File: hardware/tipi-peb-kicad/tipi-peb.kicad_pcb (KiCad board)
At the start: 2 copper layers, 237.7 x 117.3 mm, 43 parts, among them Q1 Q_NPN_BCE, U1 74HCT138, U2 27C256, U3 74HCT244, U4 74HCT244, U5 74HCT244, U6 XC95144XL-TQ100, U7 74HCT245, U8 LM1117-3.3, U9 LM7805_TO220

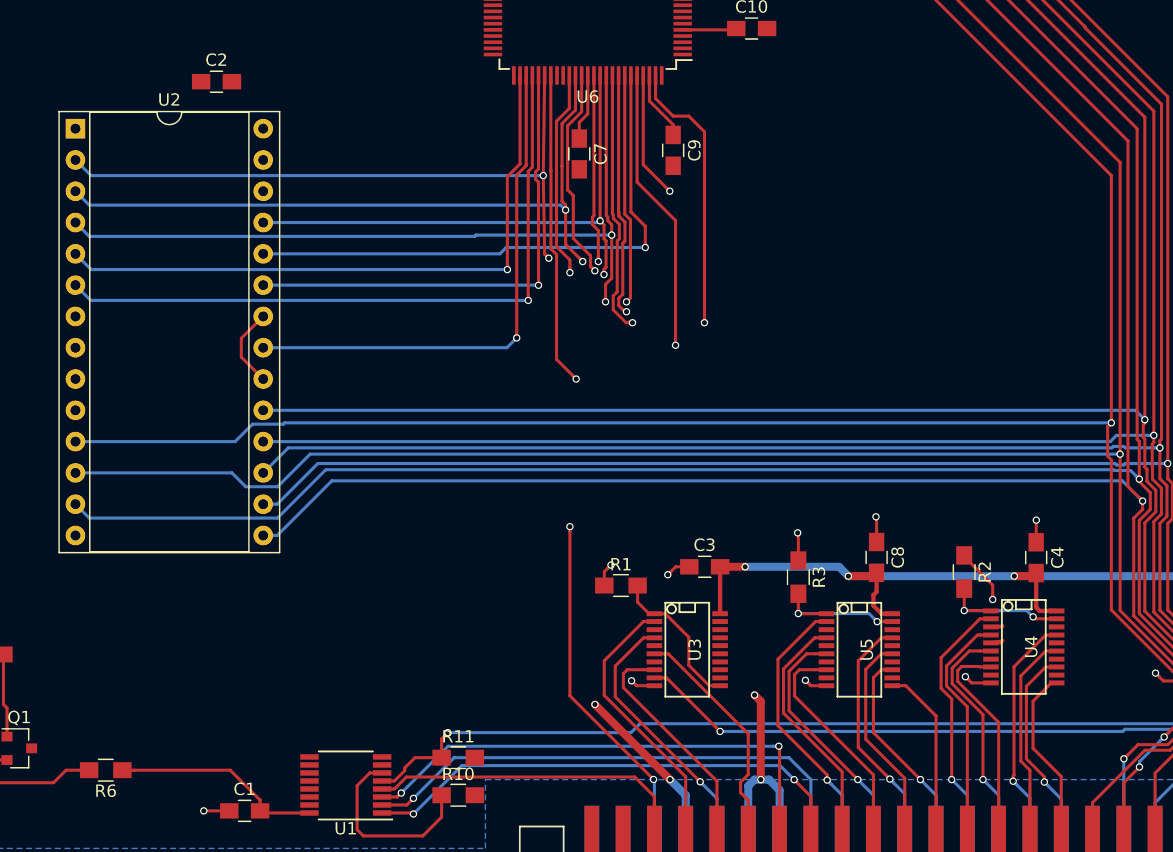
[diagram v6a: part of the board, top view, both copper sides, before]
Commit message: finish an address buffer
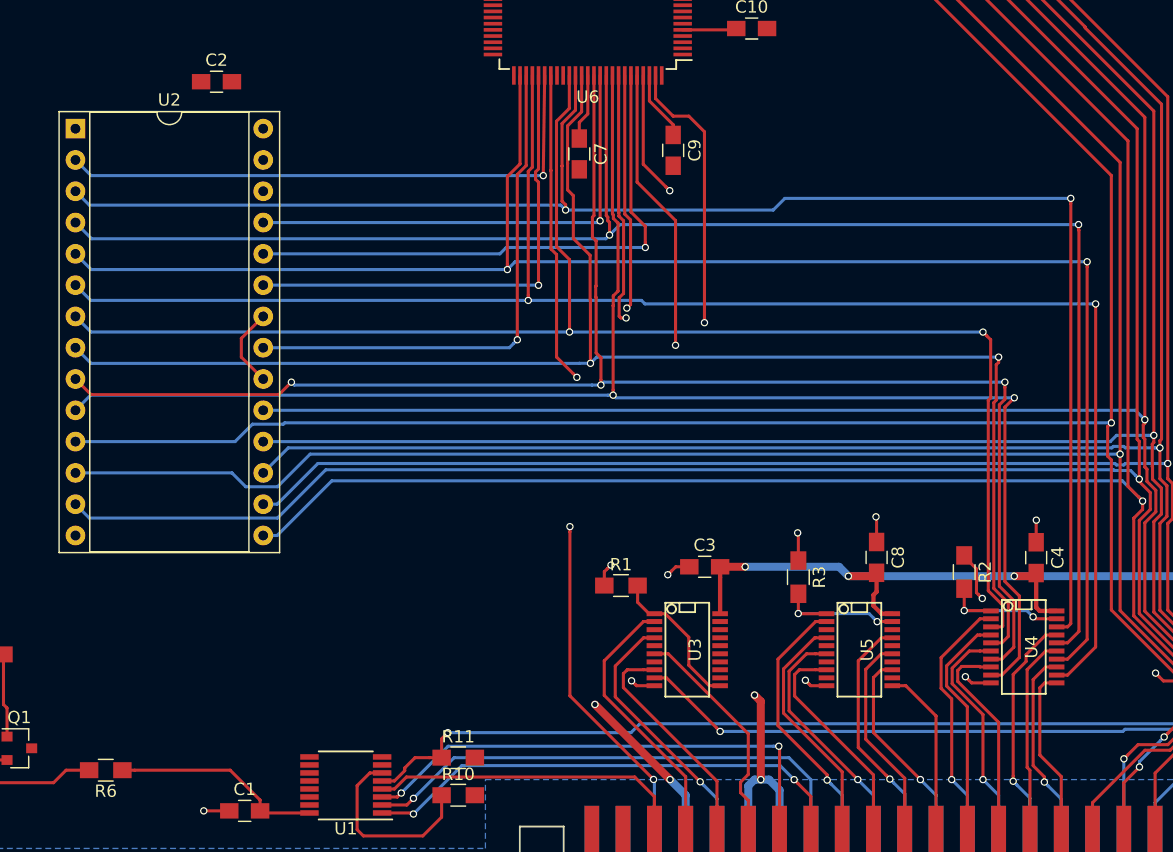
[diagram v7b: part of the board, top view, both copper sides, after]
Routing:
- net B_A14: track 15.4 -> 126.5 mm, vias 1 -> 3
- net B_A15: track 21.5 -> 127.9 mm, vias 1 -> 2
- net B_A13: track 19.2 -> 125.2 mm, vias 1 -> 2
- net B_A12: track 18.8 -> 121.6 mm, vias 1 -> 2
- net B_A10: track 51.8 -> 132.9 mm, vias 1 -> 2
- net B_A11: track 55.7 -> 133.8 mm, vias 1 -> 2
- net B_A8: track 56.7 -> 129.1 mm
- net B_A9: track 62.8 -> 130.7 mm
- net B_A3: track 53.5 -> 46.6 mm, vias 2 -> 1
- net B_A7: track 43.8 -> 39.2 mm, vias 2 -> 1
- net B_A2: track 19.9 -> 20.5 mm

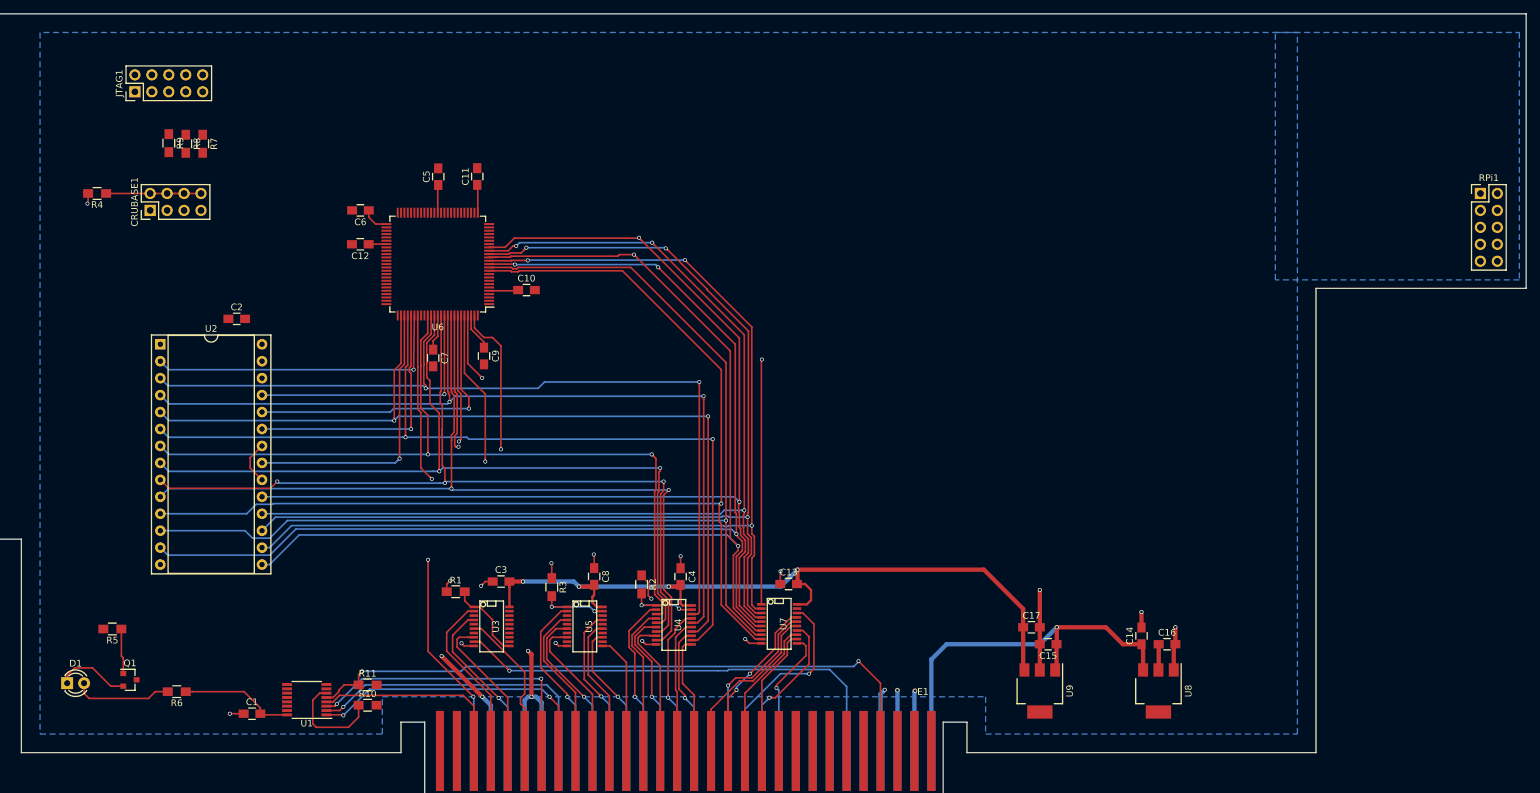
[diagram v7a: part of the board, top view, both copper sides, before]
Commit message: just power lines left
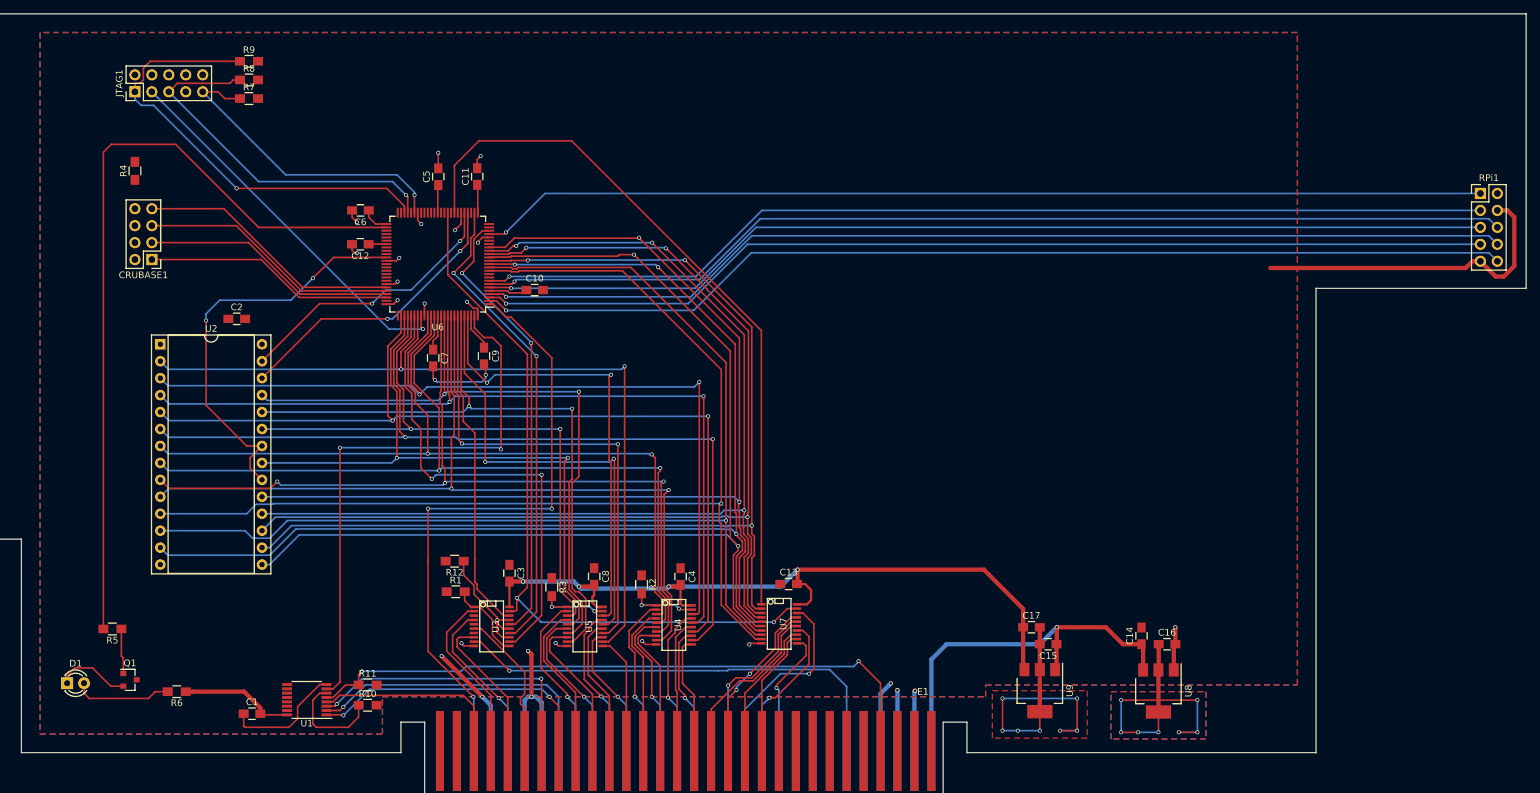
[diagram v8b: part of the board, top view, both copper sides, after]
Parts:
- added R12: 1k, Resistors_SMD:R_0805_HandSoldering, F.Cu at (168.6, 148.1)
- U8, U9: footprint TO_SOT_Packages_SMD:SOT-223 -> TO_SOT_Packages_SMD:SOT-223-3_TabPin2
- moved R9 17.2 mm to (137.7, 73.2), turned to 0 degrees
- moved R8 13.5 mm to (137.7, 75.9), turned to 0 degrees
- moved R7 9.70 mm to (137.7, 78.7), turned to 0 degrees
- moved CRUBASE1 7.37 mm to (123.2, 102.9), turned to 180 degrees
- moved R4 6.60 mm to (120.7, 89.6), turned to 90 degrees
- moved C3 1.77 mm to (176.8, 149.9), turned to 270 degrees
- moved C10 1.23 mm to (180.6, 107.4)
- moved U9 0.05 mm to (256.3, 167.5)
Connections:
- U3 pad 13: Net-(U3-Pad13) -> Net-(R12-Pad1)
- U3 pad 15: Net-(U3-Pad15) -> Net-(R12-Pad1)
- U3 pad 17: Net-(U3-Pad17) -> Net-(R12-Pad1)
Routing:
- net R_DC: track 0.00 -> 155.8 mm, vias 0 -> 1
- net R_DOUT: track 0.00 -> 155.7 mm, vias 0 -> 1
- net R_DIN: track 0.00 -> 155.6 mm, vias 0 -> 1
- net R_RT: track 0.00 -> 153.0 mm, vias 0 -> 1
- net R_RESET: track 0.00 -> 152.6 mm, vias 0 -> 1
- net R_LE: track 0.00 -> 152.4 mm, vias 0 -> 1
- net R_CLK: track 0.00 -> 151.1 mm, vias 0 -> 1
- net LED0: track 0.00 -> 119.5 mm
- net GND: track 124.7 -> 243.4 mm, vias 23 -> 33
- net DB_EN: track 0.00 -> 110.6 mm, vias 0 -> 2
- net B_A3: track 46.6 -> 122.3 mm, vias 1 -> 2
- net B_PH3: track 0.00 -> 71.7 mm, vias 0 -> 2
- net DB_DIR: track 36.7 -> 107.4 mm, vias 1 -> 0
- net JTAG_TCK: track 0.00 -> 68.5 mm, vias 0 -> 1
- net B_CRUCLK: track 0.00 -> 67.5 mm, vias 0 -> 2
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- added copper zone on B.Cu, net +3V3
- added copper zone on F.Cu, net +3V3
- added copper zone on F.Cu, net GND
